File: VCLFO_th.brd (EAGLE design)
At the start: 98.7 x 39.4 mm, 38 parts, among them IC1 LM324N, IC3 LM358N

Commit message: Updated component values of LED2 and LDR1 (Vactrol/optocoupler).
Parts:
- LDR1: value PGM55xx 18-50k e-kit 40850005 -> Token PGM5539
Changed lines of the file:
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@@
 <attribute name="VALUE" x="56.515" y="44.196" size="1.27" layer="25" ratio="10" rot="SR270"/>
 </element>
-<element name="LDR1" library="lb_devs" package="LDR_SNR2-3.0" value="PGM55xx 18-50k e-kit 40850005" x="64.77" y="27.94" smashed="yes" rot="R180">
+<element name="LDR1" library="lb_devs" package="LDR_SNR2-3.0" value="Token PGM5539" x="64.77" y="27.94" smashed="yes" rot="R180">
 <attribute name="MPN" value="PGM55xx" x="64.77" y="27.94" size="1.778" layer="27" rot="R180" display="off"/>
 <attribute name="NAME" x="67.31" y="25.4" size="0.889" layer="25" ratio="11" rot="R180"/>

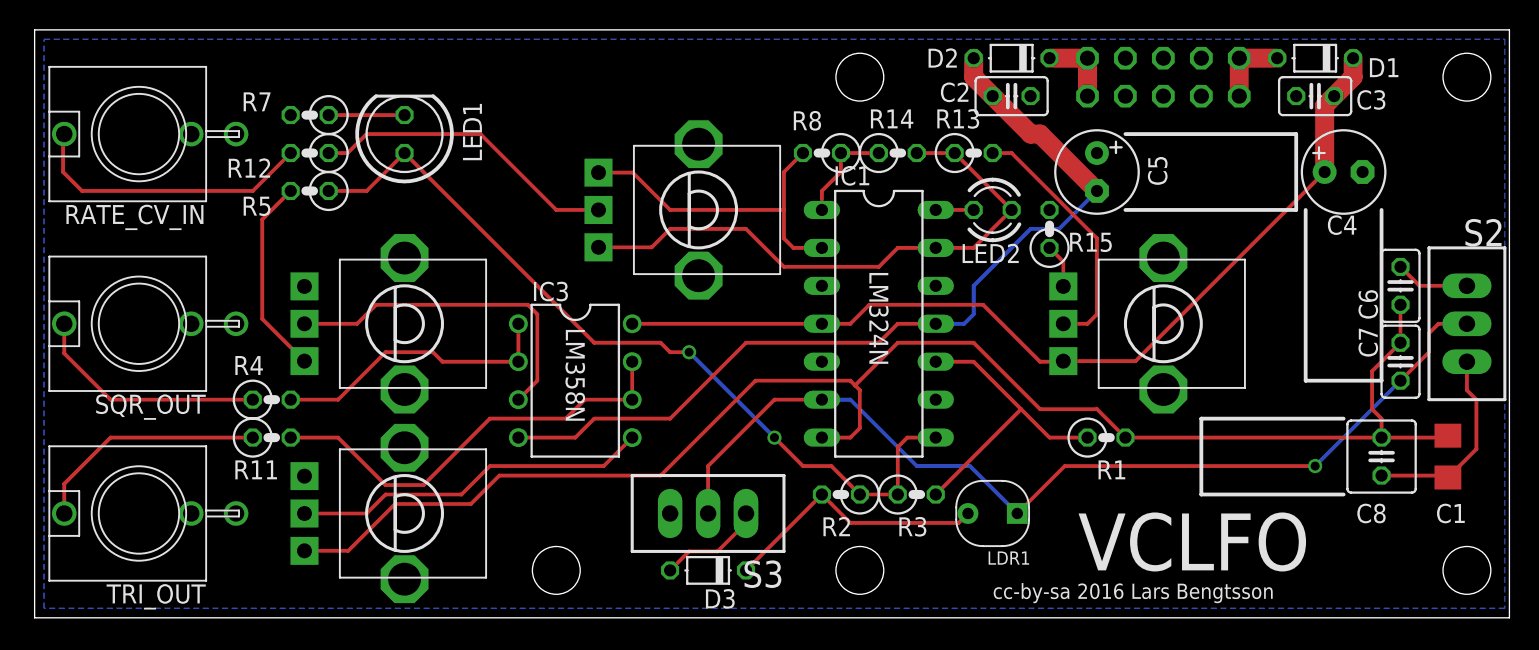
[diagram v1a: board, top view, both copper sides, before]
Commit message: Renamed IC3->IC2. Rate CV potentiometer was 1/40" off, corrected. Moved IC1 1/40" towards same pot, makes a bit more space for optical stuff. Moved R15 a bit, moved C6 and C7.
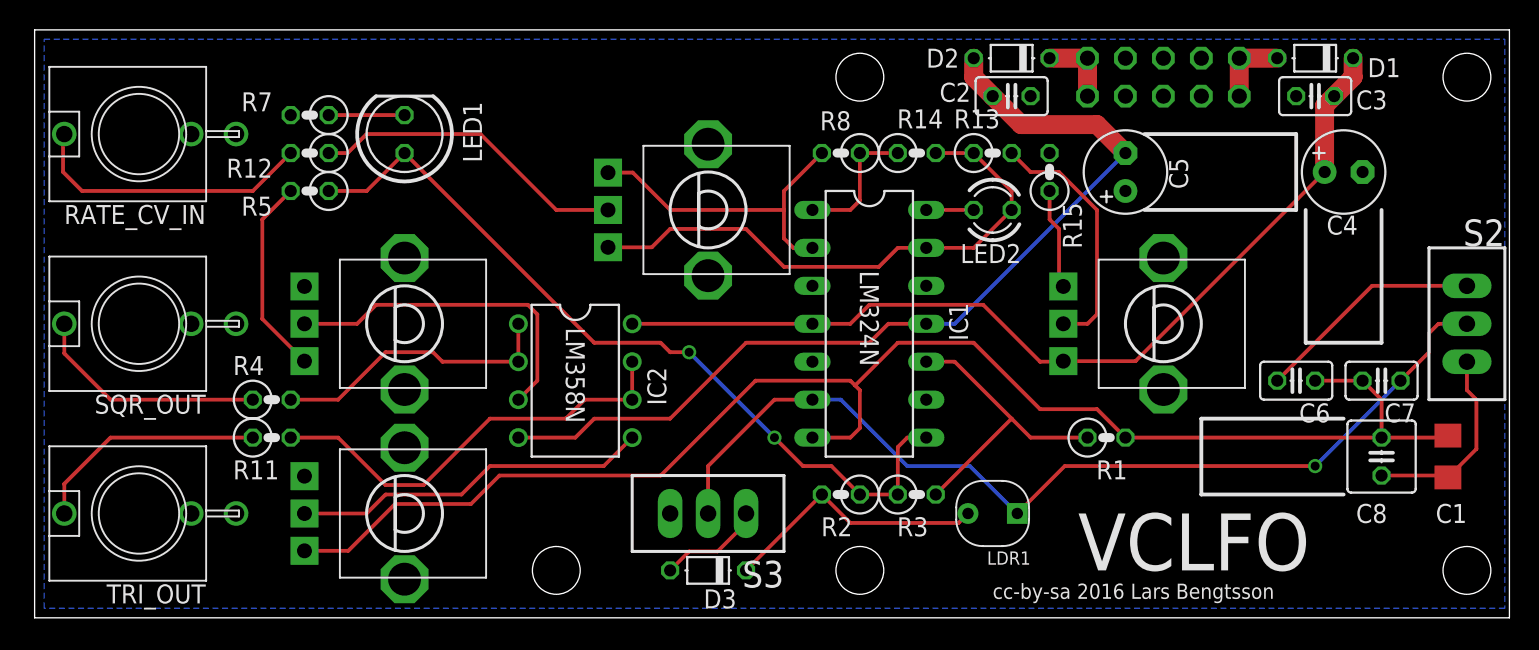
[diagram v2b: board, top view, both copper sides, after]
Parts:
- moved C6 9.44 mm to (85.1, 36.8), turned to 0 degrees
- moved R15 3.81 mm to (68.6, 50.8)
- moved C5 1.91 mm to (73.7, 50.8), turned to 90 degrees
- moved C7 1.80 mm to (90.8, 36.8), turned to 180 degrees
- moved R13 1.27 mm to (64.8, 52.1)
- moved R14 1.27 mm to (59.7, 52.1)
- moved R8 1.27 mm to (54.6, 52.1)
- moved CV_DIR 0.63 mm to (45.7, 48.3)
- moved IC1 0.63 mm to (56.5, 40.6)
- renumbered IC3 to IC2
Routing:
- net N$19: track 4.97 -> 15.3 mm
- net N$25: track 2.96 -> 6.77 mm
- net -12V: track 59.4 -> 62.1 mm
- net N$22: track 6.88 -> 9.15 mm
- net TRI: track 101.0 -> 99.2 mm
- net N$23: track 38.7 -> 37.6 mm
- net N$20: track 22.5 -> 21.8 mm
- net SQR: track 54.6 -> 54.0 mm
- net N$15: track 20.7 -> 21.3 mm
- net N$21: track 2.54 -> 3.17 mm

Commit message: Minor updates to labels.
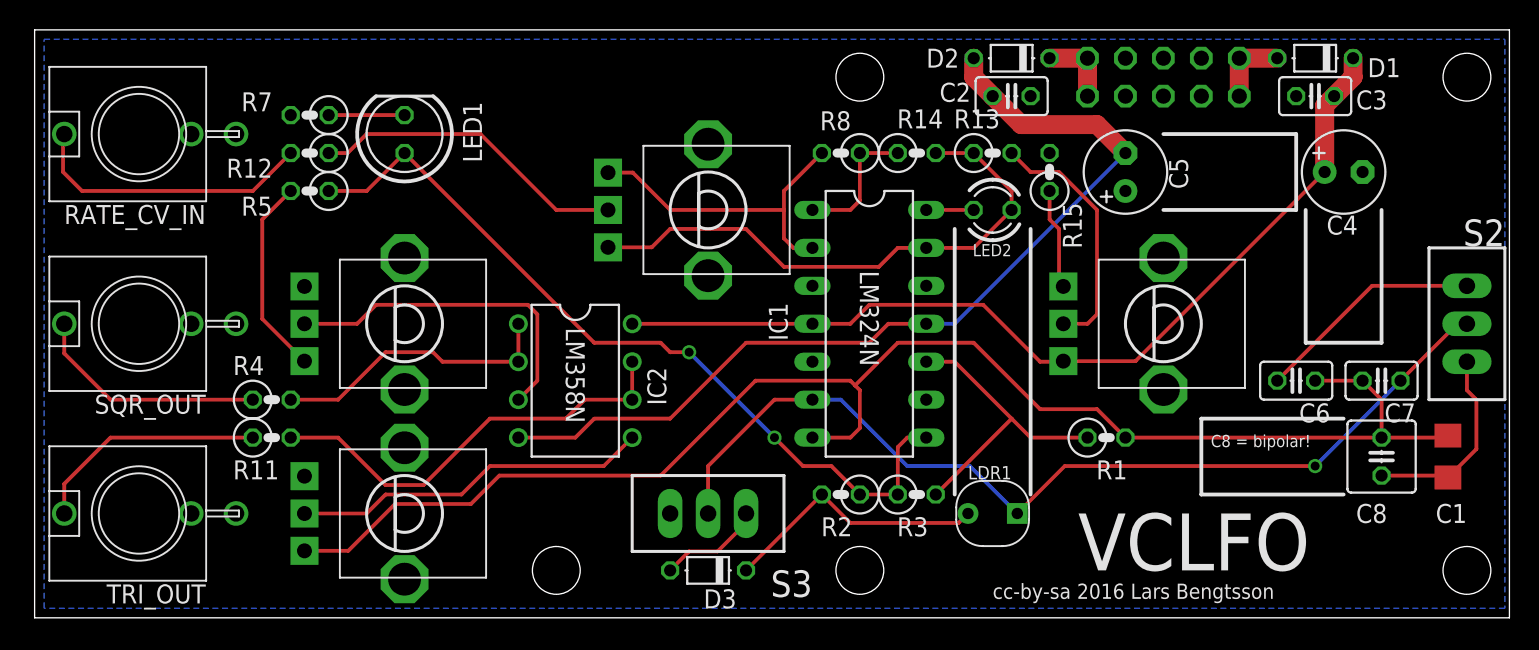
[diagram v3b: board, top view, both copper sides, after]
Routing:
- net N$1: track 65.0 -> 64.2 mm
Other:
- board text added: "C8 = bipolar!"
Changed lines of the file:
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@@
 <hole x="35.56" y="24.13" drill="3.2"/>
 <hole x="55.88" y="57.15" drill="3.2"/>
-<wire x1="74.93" y1="48.26" x2="85.09" y2="48.26" width="0.254" layer="21"/>
+<wire x1="76.2" y1="48.26" x2="85.09" y2="48.26" width="0.254" layer="21"/>
 <wire x1="85.09" y1="48.26" x2="85.09" y2="53.34" width="0.254" layer="21"/>
-<wire x1="85.09" y1="53.34" x2="74.93" y2="53.34" width="0.254" layer="21"/>
+<wire x1="85.09" y1="53.34" x2="76.2" y2="53.34" width="0.254" layer="21"/>
 <wire x1="85.725" y1="48.26" x2="85.725" y2="39.37" width="0.254" layer="21"/>
 <wire x1="85.725" y1="39.37" x2="90.805" y2="39.37" width="0.254" layer="21"/>
@@
 <text x="66.675" y="49.53" size="1.27" layer="22" font="vector" rot="SMR90">*RED
 -12V</text>
+<text x="79.375" y="32.385" size="0.8128" layer="21" font="vector">C8 = bipolar!</text>
+<wire x1="62.23" y1="46.99" x2="62.23" y2="29.21" width="0.254" layer="21"/>
+<wire x1="67.31" y1="46.99" x2="67.31" y2="29.21" width="0.254" layer="21"/>
 </plain>
 <attributes>
@@
 </element>
 <element name="IC1" library="linear" package="DIL14" value="LM324N" x="56.515" y="40.64" smashed="yes" rot="R270">
-<attribute name="NAME" x="63.119" y="39.497" size="1.27" layer="25" ratio="10" rot="R90"/>
+<attribute name="NAME" x="51.054" y="39.497" size="1.27" layer="25" ratio="10" rot="R90"/>
 <attribute name="VALUE" x="55.88" y="44.196" size="1.27" layer="25" ratio="10" rot="SR270"/>
 </element>
 <element name="LDR1" library="lb_devs" package="LDR_SNR2-3.0" value="Token PGM5539" x="64.77" y="27.94" smashed="yes" rot="R180">
 <attribute name="MPN" value="PGM55xx" x="64.77" y="27.94" size="1.778" layer="27" rot="R180" display="off"/>
-<attribute name="NAME" x="67.31" y="25.4" size="0.889" layer="25" ratio="11" rot="R180"/>
+<attribute name="NAME" x="66.04" y="31.115" size="0.889" layer="25" ratio="11" rot="R180"/>
 <attribute name="VALUE" x="67.31" y="31.115" size="0.889" layer="27" ratio="11" rot="R180"/>
 </element>
@@
 </element>
 <element name="LED2" library="led" package="LED3MM" value="" x="64.77" y="48.26" smashed="yes" rot="R180">
-<attribute name="NAME" x="66.675" y="45.974" size="1.27" layer="25" ratio="10" rot="R180"/>
+<attribute name="NAME" x="66.04" y="45.974" size="0.8128" layer="25" ratio="10" rot="R180"/>
 <attribute name="VALUE" x="62.865" y="49.911" size="1.27" layer="27" ratio="10" rot="R180"/>
 </element>
@@
 <attribute name="VALUE" x="36.195" y="40.386" size="1.27" layer="25" ratio="10" rot="SR270"/>
 </element>
-<element name="S3" library="switch" package="TL3XPO" value="SKS04SP" x="45.72" y="27.94" rot="R180"/>
+<element name="S3" library="switch" package="TL3XPO" value="SKS04SP" x="45.72" y="27.94" smashed="yes" rot="R180">
+<attribute name="NAME" x="52.705" y="24.13" size="1.778" layer="25" rot="R180"/>
+<attribute name="VALUE" x="50.8" y="33.02" size="1.778" layer="27" rot="R180"/>
+</element>
 </elements>
 <signals>
@@
 <wire x1="59.055" y1="31.115" x2="63.246" y2="31.115" width="0.254" layer="16"/>
 <wire x1="63.246" y1="31.115" x2="66.421" y2="27.94" width="0.254" layer="16"/>
-<wire x1="92.075" y1="36.83" x2="93.98" y2="38.735" width="0.254" layer="1"/>
-<wire x1="93.98" y1="38.735" x2="93.98" y2="40.005" width="0.254" layer="1"/>
-<wire x1="93.98" y1="40.005" x2="94.615" y2="40.64" width="0.254" layer="1"/>
-<wire x1="94.615" y1="40.64" x2="96.52" y2="40.64" width="0.254" layer="1"/>
+<wire x1="92.075" y1="36.83" x2="95.885" y2="40.64" width="0.254" layer="1"/>
+<wire x1="95.885" y1="40.64" x2="96.52" y2="40.64" width="0.254" layer="1"/>
 <wire x1="92.075" y1="36.83" x2="86.36" y2="31.115" width="0.254" layer="16"/>
 <via x="86.36" y="31.115" extent="1-16" drill="0.6" shape="square"/>
